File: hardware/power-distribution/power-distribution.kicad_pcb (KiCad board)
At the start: 2 copper layers, 90 x 70 mm, 25 parts, among them J1 Parallell, J2 Parallell, J3 Parallell, J4 Screw_Terminal_01x08, Q1 Q_PMOS_GDS, Q2 Q_PMOS_GDS, Q3 Q_PMOS_GDS, Q4 Q_PMOS_GDS

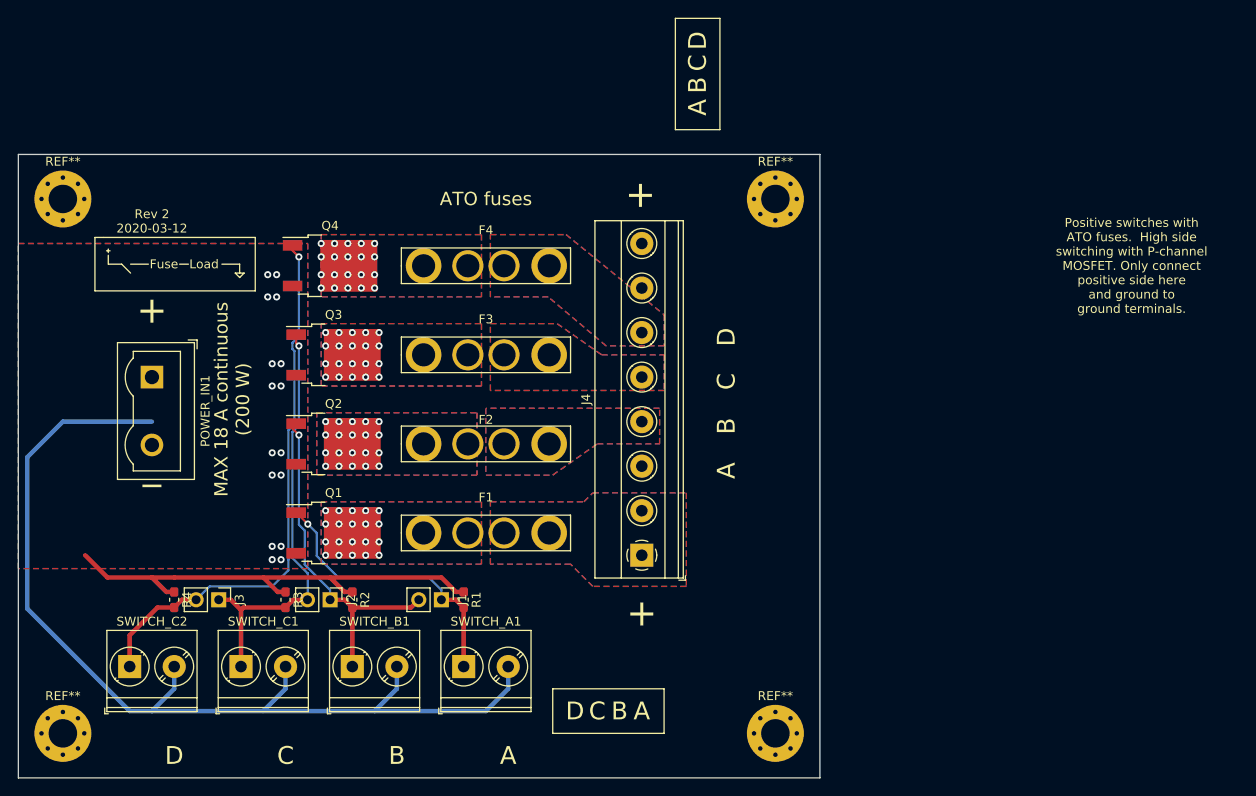
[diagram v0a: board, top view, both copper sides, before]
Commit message: Changed input connecftor to M5
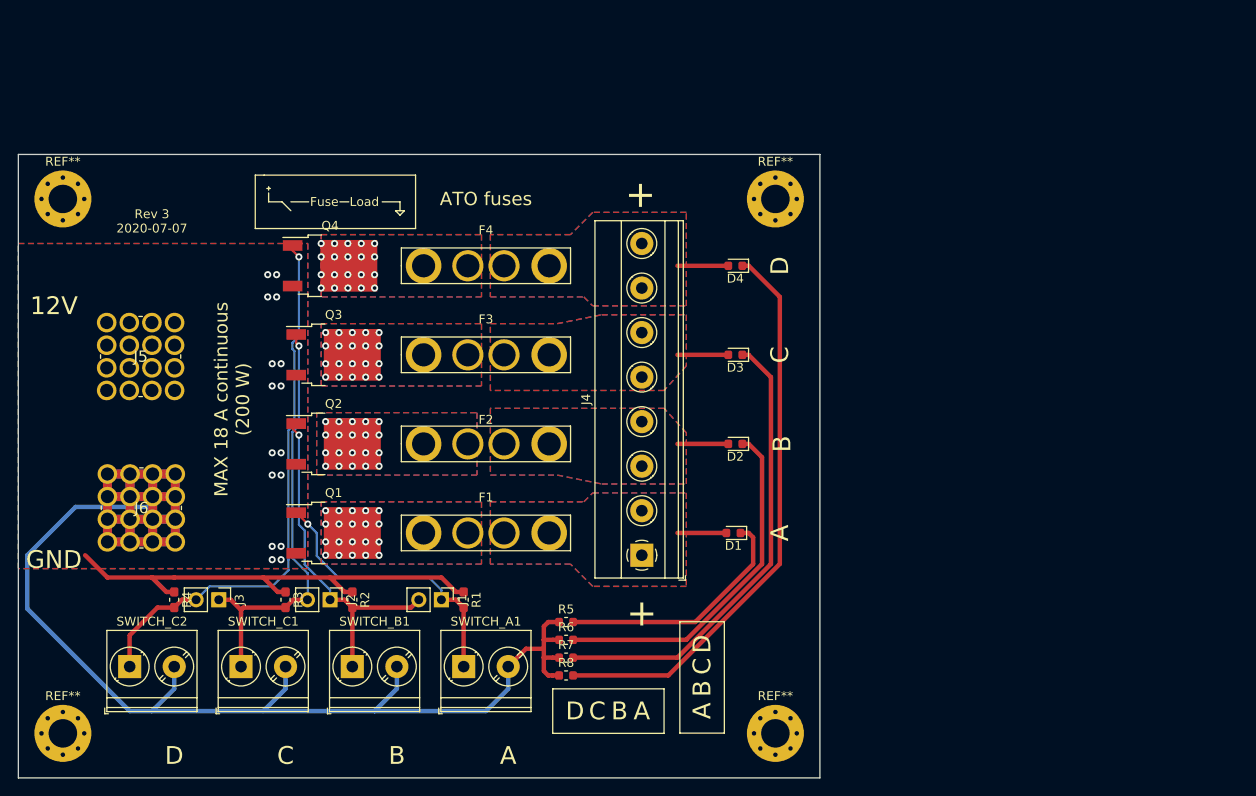
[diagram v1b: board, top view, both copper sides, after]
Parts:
- removed POWER_IN1: Screw_Terminal_01x02, TerminalBlock:TerminalBlock_Wuerth_691311400102_P7.62mm
- added D1: 2V, LED_SMD:LED_0603_1608Metric, F.Cu at (130.3, 122.5)
- added D2: 2V, LED_SMD:LED_0603_1608Metric, F.Cu at (130.5, 112.5)
- added D3: 2V, LED_SMD:LED_0603_1608Metric, F.Cu at (130.5, 102.5)
- added D4: 2V, LED_SMD:LED_0603_1608Metric, F.Cu at (130.5, 92.5)
- added J5: 12V, Private:M5_7461383, F.Cu at (59.9, 106.5)
- added J6: GND, Private:M5_7461383, F.Cu at (60.0, 123.5)
- added R5: 670R, Resistor_SMD:R_0603_1608Metric, F.Cu at (111.5, 132.5)
- added R6: 670R, Resistor_SMD:R_0603_1608Metric, F.Cu at (111.5, 134.5)
- added R7: 670R, Resistor_SMD:R_0603_1608Metric, F.Cu at (111.5, 136.5)
- added R8: 670R, Resistor_SMD:R_0603_1608Metric, F.Cu at (111.5, 138.5)
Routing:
- net GND: track 113.1 -> 241.7 mm
- net Net-(D4-Pad1): track 0.00 -> 64.0 mm
- net Net-(D3-Pad1): track 0.00 -> 51.8 mm
- net Net-(D2-Pad1): track 0.00 -> 39.6 mm
- net Net-(D1-Pad1): track 0.00 -> 27.5 mm
- net Net-(D4-Pad2): track 0.00 -> 5.71 mm
- net Net-(D3-Pad2): track 0.00 -> 5.71 mm
- net Net-(D2-Pad2): track 0.00 -> 5.71 mm
- net Net-(D1-Pad2): track 0.00 -> 5.50 mm
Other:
- board text added: "12V"
- board text added: "GND"
- board text added: "Rev 3 2020-07-07"
- board text removed: "Positive switches with ATO fuses. High side switching with P-channel MOSFET. Only connect positive side here and ground to ground terminals."
- board text removed: "Rev 2 2020-03-12"
- board text removed: "_"

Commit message: Changed to m5 connector on output
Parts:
- added J7: GND, Private:M5_7461383, F.Cu at (115.5, 117.6)
- added J8: GND, Private:M5_7461383, F.Cu at (115.5, 105.0)
- added J9: GND, Private:M5_7461383, F.Cu at (115.5, 92.5)
- J4: value Screw_Terminal_01x08 -> GND; footprint TerminalBlock_Phoenix:TerminalBlock_Phoenix_MKDS-1,5-8_1x08_P5.00mm_Horizontal -> Private:M5_7461383
- moved J4 6.79 mm to (115.5, 130.1), turned to 0 degrees
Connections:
- D1 pad 2: Net-(D1-Pad2) -> /AOUT
- D2 pad 2: Net-(D2-Pad2) -> /BOUT
- D3 pad 2: Net-(D3-Pad2) -> /COUT
- D4 pad 2: Net-(D4-Pad2) -> /DOUT
- F1 pad 1: Net-(D1-Pad2) -> /AOUT
- F2 pad 1: Net-(D2-Pad2) -> /BOUT
- F3 pad 1: Net-(D3-Pad2) -> /COUT
- F4 pad 1: Net-(D4-Pad2) -> /DOUT
- J4 pad 1: Net-(D1-Pad2) -> /AOUT
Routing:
- net Net-(D4-Pad2): track 5.71 -> 0.00 mm
- net Net-(D3-Pad2): track 5.71 -> 0.00 mm
- net Net-(D2-Pad2): track 5.71 -> 0.00 mm
- net /DOUT: track 0.00 -> 5.71 mm
- net /COUT: track 0.00 -> 5.71 mm
- net /BOUT: track 0.00 -> 5.71 mm
- net Net-(D1-Pad2): track 5.50 -> 0.00 mm
- net /AOUT: track 0.00 -> 5.50 mm
- added copper zone on B.Cu, net /AOUT
- added copper zone on F.Cu, net /AOUT
- added copper zone on B.Cu, net /BOUT
- added copper zone on F.Cu, net /BOUT
- added copper zone on B.Cu, net /COUT
- added copper zone on F.Cu, net /COUT
- added copper zone on B.Cu, net /DOUT
- added copper zone on F.Cu, net /DOUT
- removed copper zone on B.Cu, net Net-(D1-Pad2)
- removed copper zone on F.Cu, net Net-(D1-Pad2)
- removed copper zone on B.Cu, net Net-(D2-Pad2)
- removed copper zone on F.Cu, net Net-(D2-Pad2)
- removed copper zone on B.Cu, net Net-(D3-Pad2)
- removed copper zone on F.Cu, net Net-(D3-Pad2)
- removed copper zone on B.Cu, net Net-(D4-Pad2)
- removed copper zone on F.Cu, net Net-(D4-Pad2)
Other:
- board text added: "Rev 4 2020-07-30"
- board text removed: "Rev 3 2020-07-07"

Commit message: Changed to M5 connector for everything
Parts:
- F1, F2, F3, F4: footprint Private Fuses:ATO_Fuseholder_3522-2 -> fuses:ATO_Fuseholder_3522-2
